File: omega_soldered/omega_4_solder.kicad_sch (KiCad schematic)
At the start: 76 parts, among them J1 Conn_01x02_Female, U1 ProMicro

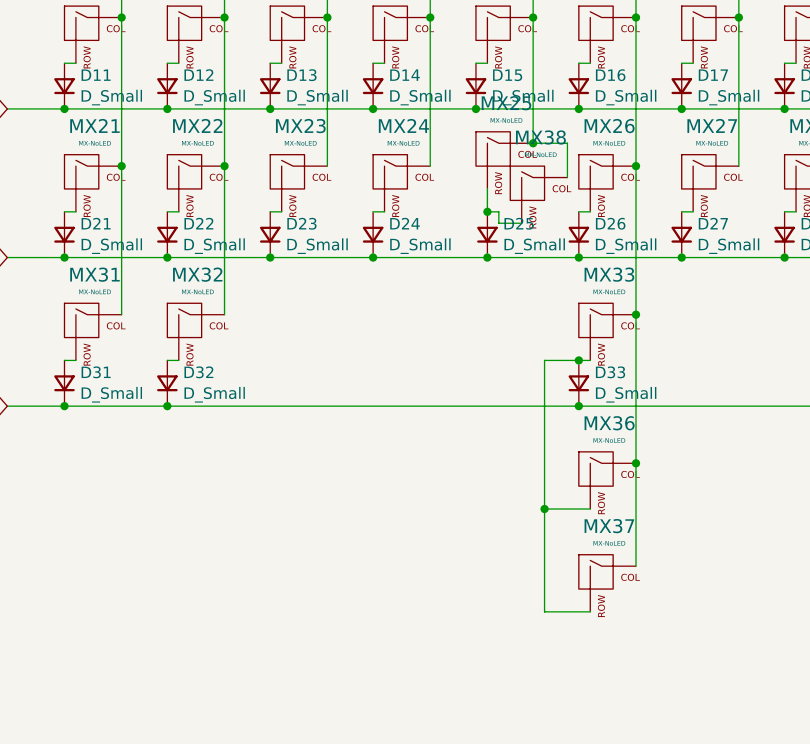
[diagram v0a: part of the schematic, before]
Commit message: add split spacebar to breakaway row
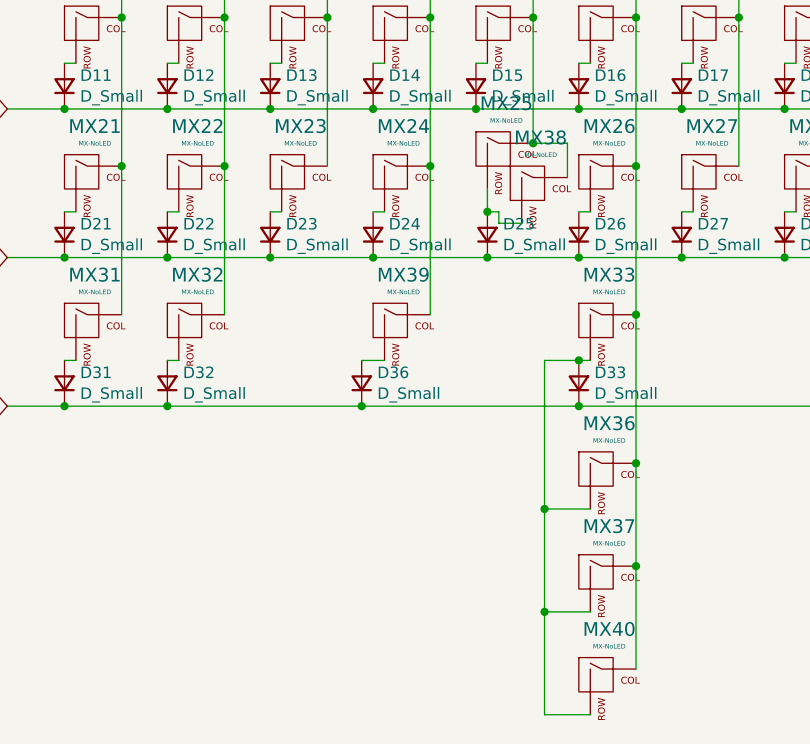
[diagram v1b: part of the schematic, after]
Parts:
- added D36: D_Small, Keebio-Parts:Diode-Hybrid-Back, symbol Device:D_Small
- added MX39, MX40: MX-NoLED, MX_Only:MXOnly-3U-ReversedStabilizers-NoLED, symbol MX_Alps_Hybrid:MX-NoLED
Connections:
- net COL3: now also MX39.1 (COL)
- net COL5: now also MX40.1 (COL)
- net ROW3: now also D36.1 (K)
- net at D33.2 (A), MX33.2 (ROW), MX36.2 (ROW)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: now also MX40.2 (ROW)
- new net: D36.2 (A), MX39.2 (ROW)
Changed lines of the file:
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@@
 (kicad_sch (version 20211123) (generator eeschema)
   (paper "A4")
+  (junction (at 218.44 111.76) (diameter 0) (color 0 0 0 0)
+  )
   (junction (at 161.29 34.29) (diameter 0) (color 0 0 0 0)
   )
@@
   (junction (at 252.73 50.8) (diameter 0) (color 0 0 0 0)
   )
+  (junction (at 187.96 93.98) (diameter 0) (color 0 0 0 0)
+  )
   (junction (at 166.37 60.96) (diameter 0) (color 0 0 0 0)
   )
@@
   (junction (at 184.15 34.29) (diameter 0) (color 0 0 0 0)
   )
+  (junction (at 195.58 67.31) (diameter 0) (color 0 0 0 0)
+  )
   (junction (at 229.87 50.8) (diameter 0) (color 0 0 0 0)
   )
@@
   )
   (junction (at 246.38 77.47) (diameter 0) (color 0 0 0 0)
+  )
+  (junction (at 208.28 116.84) (diameter 0) (color 0 0 0 0)
   )
   (junction (at 212.09 88.9) (diameter 0) (color 0 0 0 0)
@@
     (stroke (width 0) (type default) (color 0 0 0 0))
   )
+  (wire (pts (xy 195.58 67.31) (xy 195.58 83.82))
+    (stroke (width 0) (type default) (color 0 0 0 0))
+  )
   (wire (pts (xy 177.8 60.96) (xy 189.23 60.96))
     (stroke (width 0) (type default) (color 0 0 0 0))
@@
     (stroke (width 0) (type default) (color 0 0 0 0))
   )
+  (wire (pts (xy 208.28 128.27) (xy 208.28 116.84))
+    (stroke (width 0) (type default) (color 0 0 0 0))
+  )
   (wire (pts (xy 172.72 34.29) (xy 172.72 50.8))
     (stroke (width 0) (type default) (color 0 0 0 0))
@@
     (stroke (width 0) (type default) (color 0 0 0 0))
   )
+  (wire (pts (xy 218.44 111.76) (xy 218.44 123.19))
+    (stroke (width 0) (type default) (color 0 0 0 0))
+  )
   (wire (pts (xy 167.64 72.39) (xy 166.37 72.39))
     (stroke (width 0) (type default) (color 0 0 0 0))
@@
     (stroke (width 0) (type default) (color 0 0 0 0))
   )
+  (wire (pts (xy 213.36 128.27) (xy 208.28 128.27))
+    (stroke (width 0) (type default) (color 0 0 0 0))
+  )
   (wire (pts (xy 247.65 39.37) (xy 246.38 39.37))
     (stroke (width 0) (type default) (color 0 0 0 0))
@@
     (stroke (width 0) (type default) (color 0 0 0 0))
   )
-  (wire (pts (xy 212.09 93.98) (xy 166.37 93.98))
+  (wire (pts (xy 212.09 93.98) (xy 187.96 93.98))
     (stroke (width 0) (type default) (color 0 0 0 0))
   )
@@
     (stroke (width 0) (type default) (color 0 0 0 0))
   )
+  (wire (pts (xy 187.96 88.9) (xy 190.5 88.9))
+    (stroke (width 0) (type default) (color 0 0 0 0))
+  )
   (wire (pts (xy 195.58 34.29) (xy 195.58 50.8))
     (stroke (width 0) (type default) (color 0 0 0 0))
@@
   )
   (wire (pts (xy 201.93 77.47) (xy 212.09 77.47))
+    (stroke (width 0) (type default) (color 0 0 0 0))
+  )
+  (wire (pts (xy 166.37 93.98) (xy 187.96 93.98))
     (stroke (width 0) (type default) (color 0 0 0 0))
   )
@@
     (pin "1")
   )
+  (symbol (lib_id "Device:D_Small") (at 187.96 91.44 90) (unit 1)
+    (in_bom yes) (on_board yes)
+    (property "Reference" "D36" (id 0) (at 189.6872 90.2716 90)
+      (effects (font (size 1.27 1.27)) (justify right))
+    )
+    (property "Value" "D_Small" (id 1) (at 189.6872 92.583 90)
+      (effects (font (size 1.27 1.27)) (justify right))
+    )
+    (property "Footprint" "Keebio-Parts:Diode-Hybrid-Back" (id 2) (at 187.96 91.44 90)
+      (effects (font (size 1.27 1.27)) hide)
+    )
+    (property "Datasheet" "~" (id 3) (at 187.96 91.44 90)
+      (effects (font (size 1.27 1.27)) hide)
+    )
+    (pin "1")
+    (pin "2")
+  )
+  (symbol (lib_id "MX_Alps_Hybrid:MX-NoLED") (at 191.77 85.09 0) (unit 1)
+    (in_bom yes) (on_board yes)
+    (property "Reference" "MX39" (id 0) (at 192.6082 79.4258 0)
+      (effects (font (size 1.524 1.524)))
+    )
+    (property "Value" "MX-NoLED" (id 1) (at 192.6082 81.3054 0)
+      (effects (font (size 0.508 0.508)))
+    )
+    (property "Footprint" "MX_Only:MXOnly-3U-ReversedStabilizers-NoLED" (id 2) (at 175.895 85.725 0)
+      (effects (font (size 1.524 1.524)) hide)
+    )
+    (property "Datasheet" "" (id 3) (at 175.895 85.725 0)
+      (effects (font (size 1.524 1.524)) hide)
+    )
+    (pin "1")
+    (pin "2")
+  )
+  (symbol (lib_id "MX_Alps_Hybrid:MX-NoLED") (at 214.63 124.46 0) (unit 1)
+    (in_bom yes) (on_board yes)
+    (property "Reference" "MX40" (id 0) (at 215.4682 118.7958 0)
+      (effects (font (size 1.524 1.524)))
+    )
+    (property "Value" "MX-NoLED" (id 1) (at 215.4682 120.6754 0)
+      (effects (font (size 0.508 0.508)))
+    )
+    (property "Footprint" "MX_Only:MXOnly-3U-ReversedStabilizers-NoLED" (id 2) (at 198.755 125.095 0)
+      (effects (font (size 1.524 1.524)) hide)
+    )
+    (property "Datasheet" "" (id 3) (at 198.755 125.095 0)
+      (effects (font (size 1.524 1.524)) hide)
+    )
+    (pin "1")
+    (pin "2")
+  )
   (symbol (lib_id "Connector:Conn_01x02_Female") (at 124.46 82.55 0) (unit 1)
     (in_bom yes) (on_board yes) (fields_autoplaced)
@@
       (reference "D35") (unit 1) (value "D_Small") (footprint "Keebio-Parts:Diode-Hybrid-Back")
     )
+    (path "/458f6a71-864e-4de4-89d3-b64dbe58310b"
+      (reference "D36") (unit 1) (value "D_Small") (footprint "Keebio-Parts:Diode-Hybrid-Back")
+    )
     (path "/c9488fb0-c52e-4f42-99a0-b4dc07fc41dc"
       (reference "J1") (unit 1) (value "Conn_01x02_Female") (footprint "Connector_PinHeader_2.00mm:PinHeader_1x02_P2.00mm_Vertical")
@@
       (reference "MX38") (unit 1) (value "MX-NoLED") (footprint "MX_Only:MXOnly-2U-ReversedStabilizers-NoLED")
     )
+    (path "/57777f77-c29c-4626-b676-5db1b6375a5f"
+      (reference "MX39") (unit 1) (value "MX-NoLED") (footprint "MX_Only:MXOnly-3U-ReversedStabilizers-NoLED")
+    )
+    (path "/6724d18b-2934-4430-98a8-ebcd97522ce0"
+      (reference "MX40") (unit 1) (value "MX-NoLED") (footprint "MX_Only:MXOnly-3U-ReversedStabilizers-NoLED")
+    )
     (path "/00000000-0000-0000-0000-00005ed6f60f"
